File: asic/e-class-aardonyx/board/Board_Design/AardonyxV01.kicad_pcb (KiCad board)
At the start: 4 copper layers, 157.5 x 117.3 mm, 327 parts, among them J1 USB_B_6PIN, J10 Conn_1x6, J11 Conn_1x6, J12 Conn_1x3_M, J13 Conn_1x8_F, J14 Conn_1x6_F, J15 Conn_1x10_F, J16 Conn_1x8_F, J17 USB_OTG, J18 Conn_1x3_M, J19 Conn_1x3_M, J2 Conn_1x8, J3 Conn_1x3_M, J4 Conn_1x4, J5 PJ-202H PWRJACK, J6 Conn_1x3_M, J7 Conn_1x4, J8 Conn_1x3_M, J9 Conn_1x8, Q1 FDN339AN, SW1 SW_SPST, SW2 FSM2JSMAATR, SW3 SW_DIP_x03, U1 FT2232H, U10 TPS7A7002DDAR, U11 ADM1186, U13 TPS7A7002DDAR, U14 74AUP1G09GW, U15 SKT32E, U16 93LC56BT-I_OT, U2 IS42S32160F-TSOP2, U3 CDCE913PW, U4 TPS54627DDAR, U5 CAT24M01WI-GT3, U6 IS25LP256x-xM, U7 ADC128S102CIMTX/NOPB, U8 LSF0108PWR, U9 LSF0108PWR, Y1 12MHz, Y2 27MHz

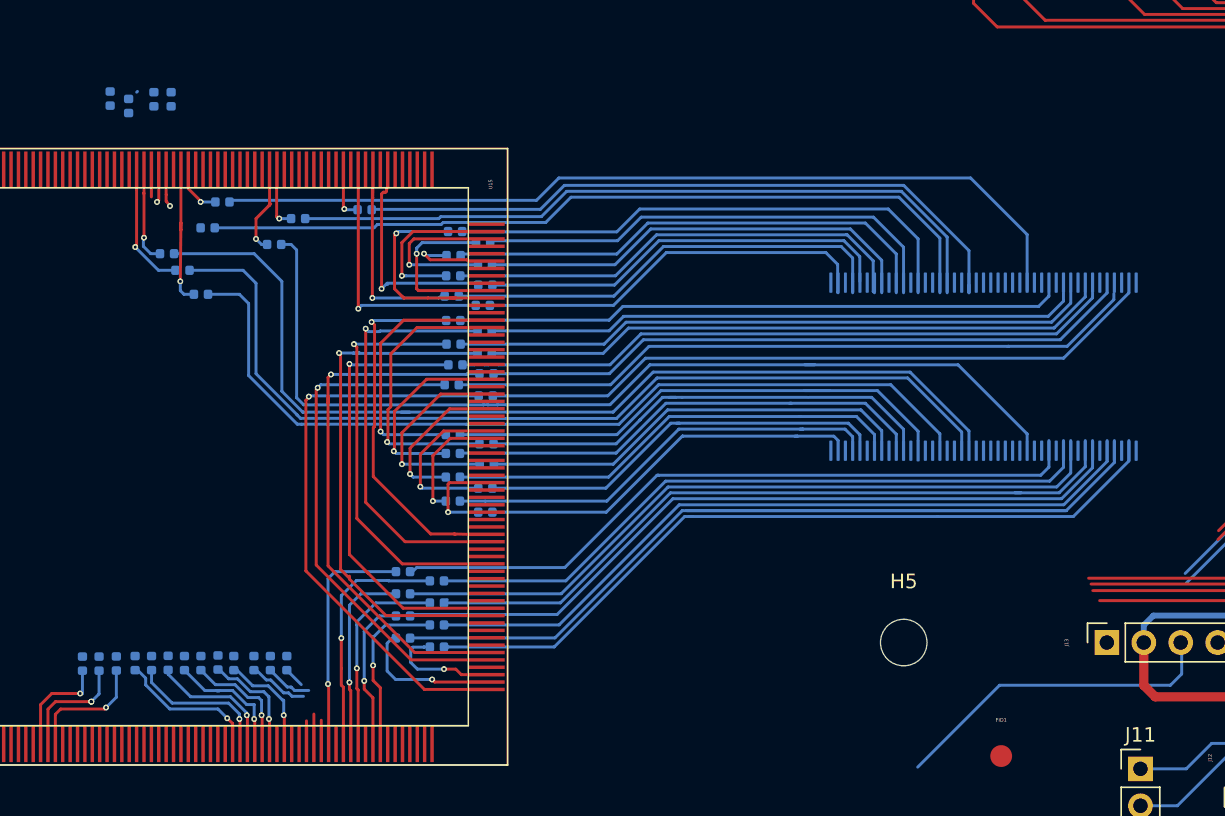
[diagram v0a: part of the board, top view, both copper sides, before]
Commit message: RAM routing update
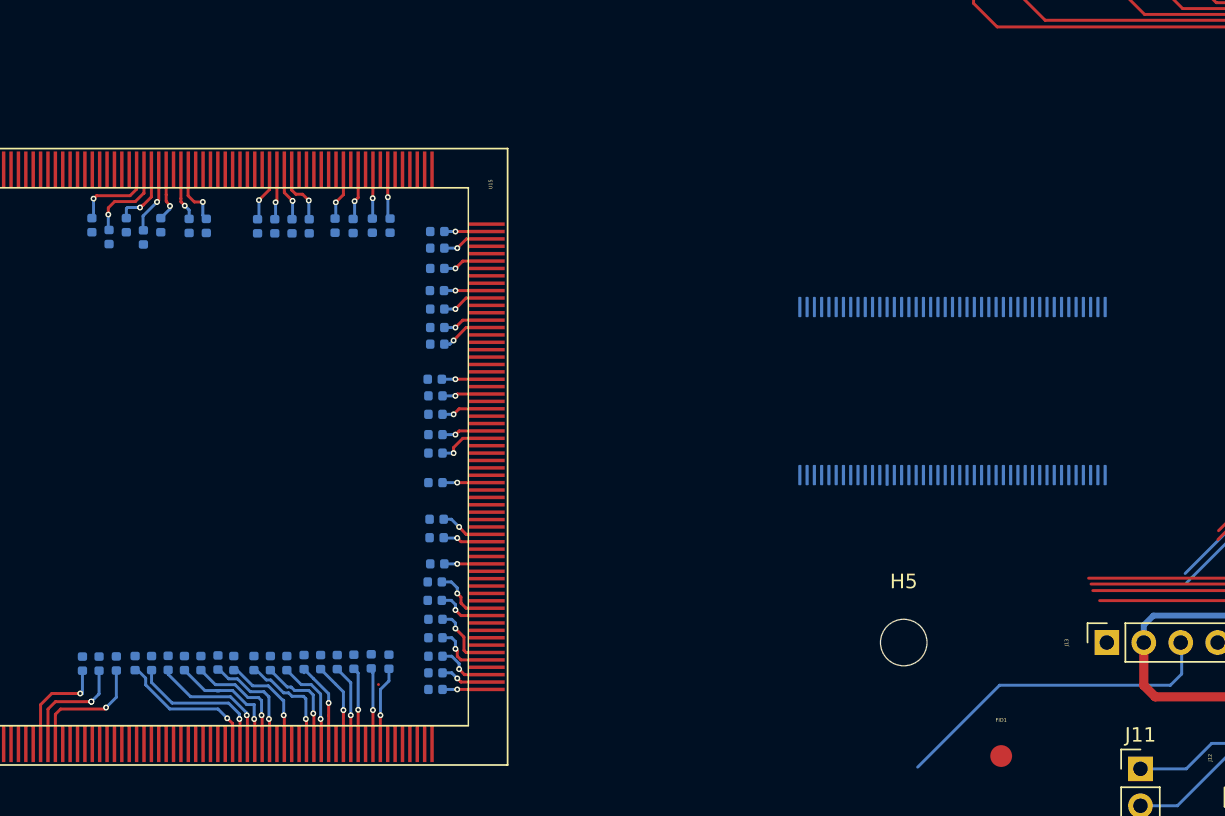
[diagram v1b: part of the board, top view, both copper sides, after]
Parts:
- moved R119 20.5 mm to (189.0, 102.5), turned to 0 degrees
- moved R118 17.4 mm to (189.0, 98.9), turned to 0 degrees
- moved R115 17.3 mm to (189.0, 96.4), turned to 0 degrees
- moved R117 17.3 mm to (189.0, 97.7), turned to 0 degrees
- moved R114 15.2 mm to (189.1, 93.9), turned to 0 degrees
- moved R116 15.0 mm to (189.0, 95.1), turned to 0 degrees
- moved R113 14.6 mm to (189.1, 92.1), turned to 0 degrees
- moved R112 13.7 mm to (189.1, 90.8), turned to 0 degrees
- moved R85 12.9 mm to (180.3, 70.6)
- moved R86 12.9 mm to (179.1, 70.6)
- moved R96 10.5 mm to (183.3, 70.6), turned to 90 degrees
- moved R126 9.75 mm to (181.1, 100.6), turned to 270 degrees
- moved R127 9.22 mm to (180.0, 100.6), turned to 270 degrees
- moved R83 9.10 mm to (168.9, 71.4)
- moved R82 8.78 mm to (167.7, 70.6)
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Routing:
- net /sdram/SDRAM_D25: track 81.1 -> 0.00 mm
- net /sdram/SDRAM_CKE: track 67.7 -> 0.00 mm
- net /sdram/SDRAM_DQM3: track 66.1 -> 0.00 mm
- net /sdram/SDRAM_CLK: track 64.3 -> 0.00 mm
- net /sdram/SDRAM_DQM2: track 61.0 -> 0.00 mm
- net /sdram/SDRAM_DQM1: track 59.9 -> 0.00 mm
- net /sdram/SDRAM_DQM0: track 55.7 -> 0.00 mm
- net /sdram/SDRAM_D24: track 54.3 -> 0.00 mm
- net /sdram/SDRAM_D27: track 53.0 -> 0.00 mm
- net /sdram/SDRAM_D26: track 52.0 -> 0.00 mm
- net /sdram/SDRAM_D29: track 51.1 -> 0.00 mm
- net /sdram/SDRAM_D28: track 50.5 -> 0.00 mm
- net /sdram/SDRAM_WE: track 50.1 -> 0.00 mm
- net /sdram/SDRAM_D31: track 48.8 -> 0.00 mm
- net /sdram/SDRAM_D22: track 47.8 -> 0.00 mm
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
